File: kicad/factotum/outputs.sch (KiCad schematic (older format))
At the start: 69 parts, among them J10 OUT3, J11 OUT5, J12 OUT7, J13 Conn_01x10_Female, J14 OUT2, J15 OUT4, J16 OUT6, J17 OUT8, J18 Conn_01x10_Male, J19 Conn_01x18_Female, J20 Conn_01x18_Male, J9 OUT1, U10 DAC128S085, U15 PCA9685PW, U6 LM2902, U7 LM2902

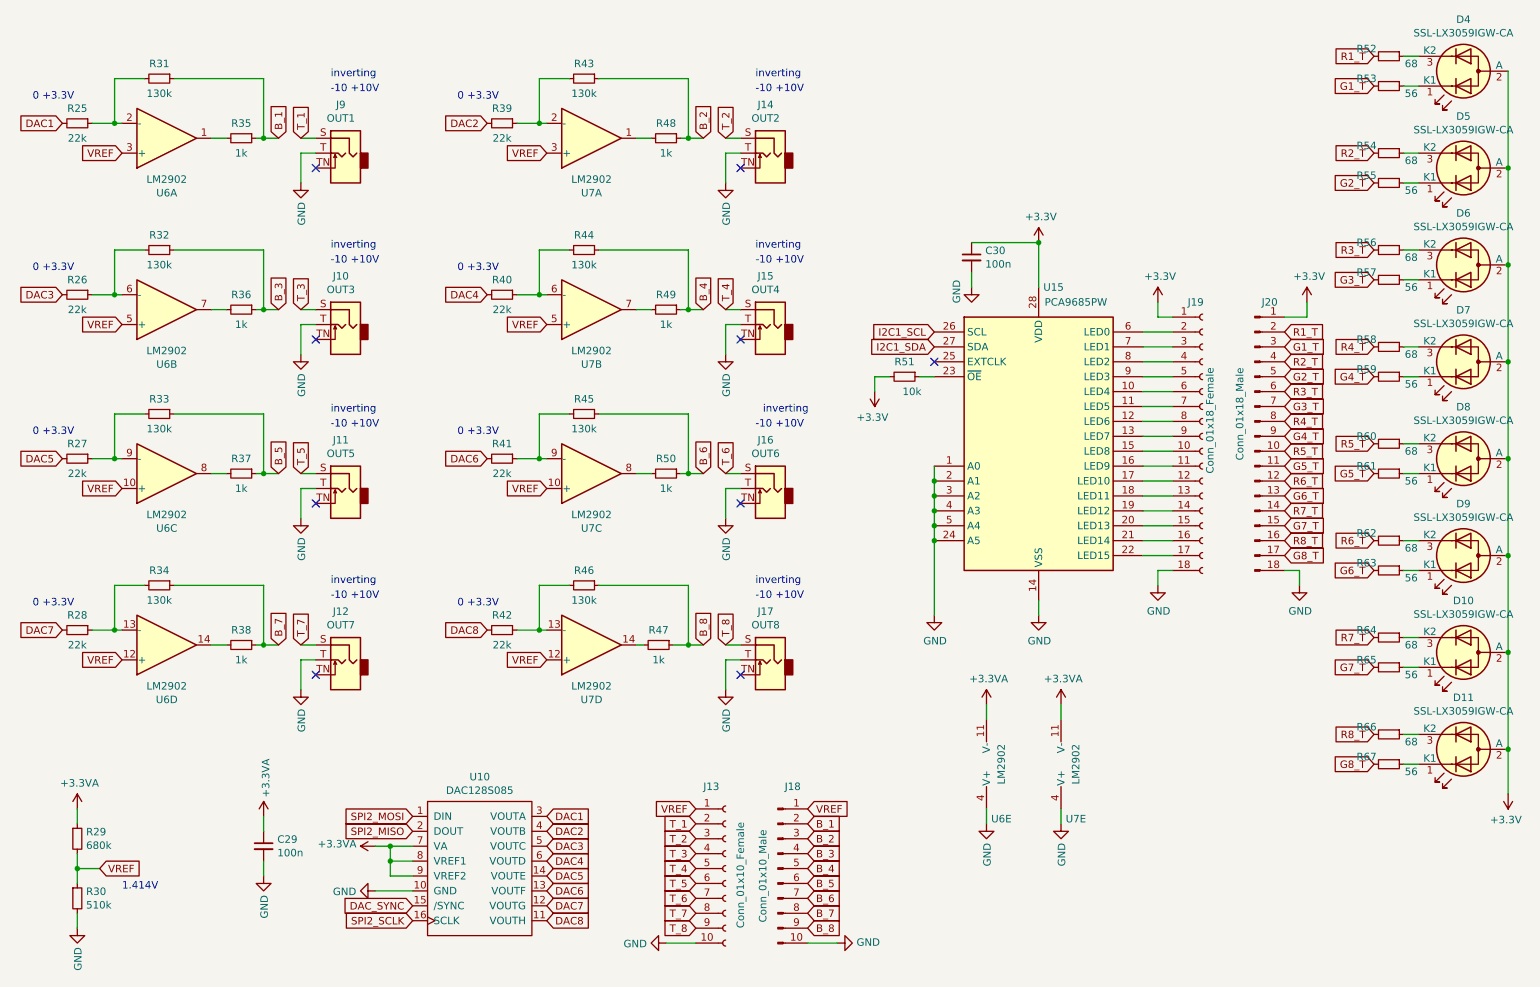
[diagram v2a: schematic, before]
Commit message: inital board layout done but not routed
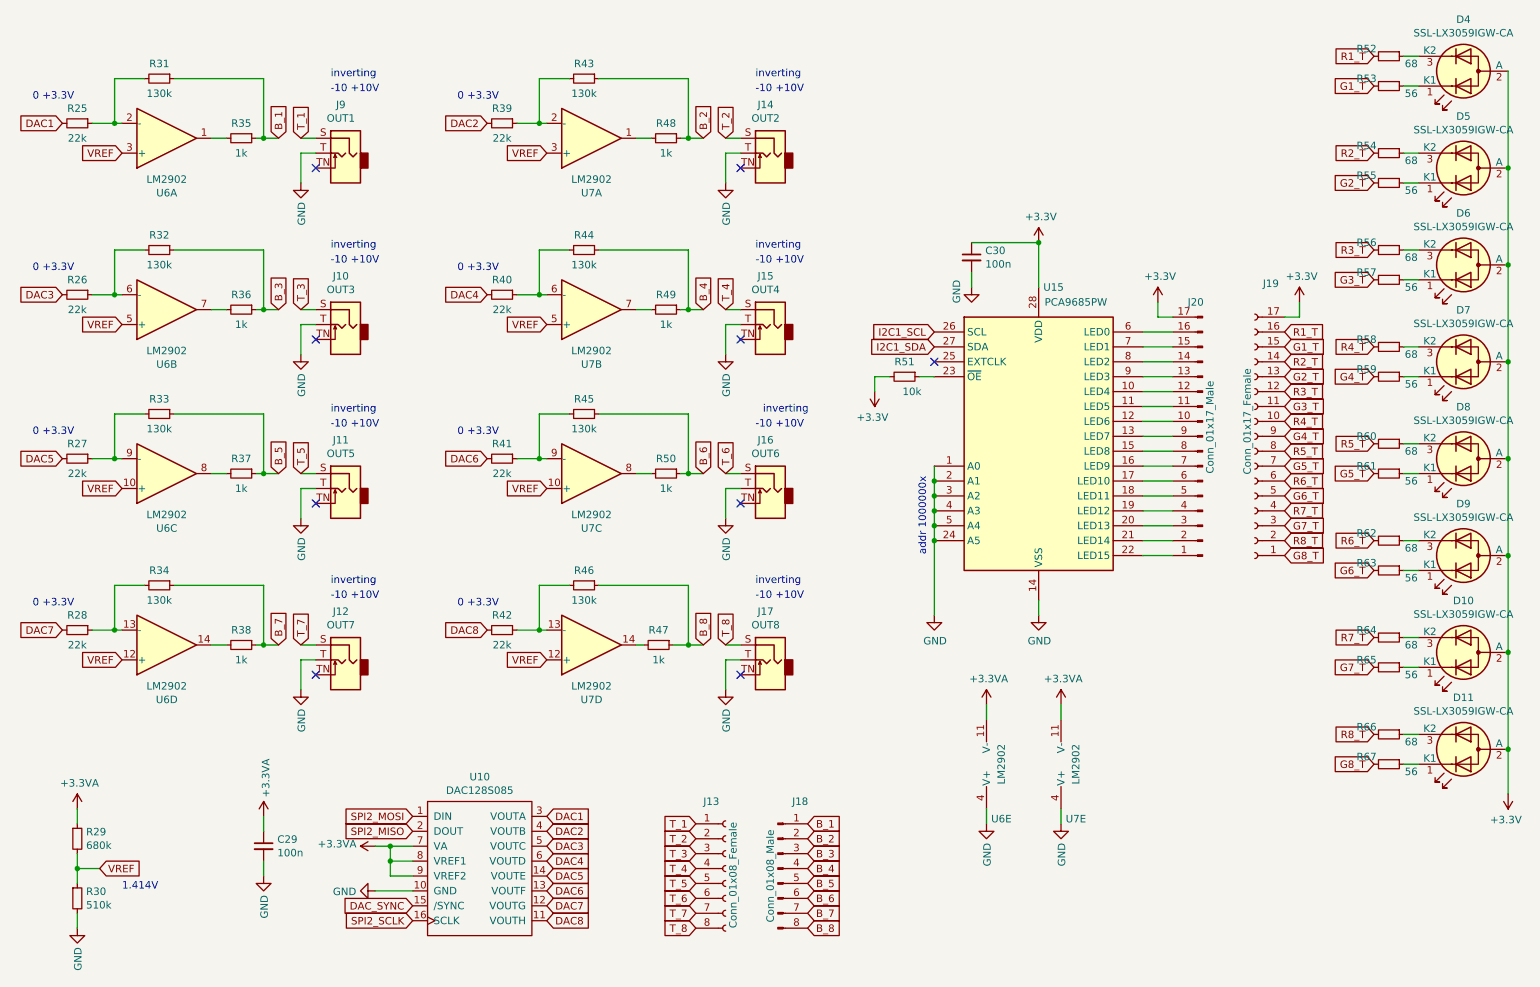
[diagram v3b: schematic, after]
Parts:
- removed J13: Conn_01x10_Female, Connector_PinSocket_1.27mm:PinSocket_1x10_P1.27mm_Vertical, symbol Connector:Conn_01x10_Female
- removed J18: Conn_01x10_Male, Connector_PinHeader_1.27mm:PinHeader_1x10_P1.27mm_Vertical, symbol Connector:Conn_01x10_Male
- removed J19: Conn_01x18_Female, Connector_PinSocket_1.27mm:PinSocket_1x18_P1.27mm_Vertical, symbol Connector:Conn_01x18_Female
- removed J20: Conn_01x18_Male, Connector_PinHeader_1.27mm:PinHeader_1x18_P1.27mm_Vertical, symbol Connector:Conn_01x18_Male
- added J13: Conn_01x08_Female, Connector_PinSocket_2.54mm:PinSocket_1x08_P2.54mm_Vertical, symbol Connector:Conn_01x08_Female
- added J18: Conn_01x08_Male, Connector_PinHeader_2.54mm:PinHeader_1x08_P2.54mm_Vertical, symbol Connector:Conn_01x08_Male
- added J19: Conn_01x17_Female, Connector_PinSocket_2.54mm:PinSocket_1x17_P2.54mm_Vertical, symbol Connector:Conn_01x17_Female
- added J20: Conn_01x17_Male, Connector_PinHeader_2.54mm:PinHeader_1x17_P2.54mm_Vertical, symbol Connector:Conn_01x17_Male
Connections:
- net +3V3: now also J19.17 (Pin_17), J20.17 (Pin_17)
- net B_1: now also J18.1 (Pin_1)
- net B_2: now also J18.2 (Pin_2)
- net B_3: now also J18.3 (Pin_3)
- net B_4: now also J18.4 (Pin_4)
- net B_5: now also J18.5 (Pin_5)
- net B_6: now also J18.6 (Pin_6)
- net B_7: now also J18.7 (Pin_7)
- net B_8: now also J18.8 (Pin_8)
- net G1_T: now also J19.15 (Pin_15)
- net G2_T: now also J19.13 (Pin_13)
- net G3_T: now also J19.11 (Pin_11)
- net G4_T: now also J19.9 (Pin_9)
- net G5_T: now also J19.7 (Pin_7)
- net G6_T: now also J19.5 (Pin_5)
- net G7_T: now also J19.3 (Pin_3)
- net G8_T: now also J19.1 (Pin_1)
- net R1_T: now also J19.16 (Pin_16)
- net R2_T: now also J19.14 (Pin_14)
- net R3_T: now also J19.12 (Pin_12)
- net R4_T: now also J19.10 (Pin_10)
- net R5_T: now also J19.8 (Pin_8)
- net R6_T: now also J19.6 (Pin_6)
- net R7_T: now also J19.4 (Pin_4)
- net R8_T: now also J19.2 (Pin_2)
- net T_1: now also J13.1 (Pin_1)
- net T_2: now also J13.2 (Pin_2)
- net T_3: now also J13.3 (Pin_3)
- net T_4: now also J13.4 (Pin_4)
- net T_5: now also J13.5 (Pin_5)
- net T_6: now also J13.6 (Pin_6)
- net T_7: now also J13.7 (Pin_7)
- net T_8: now also J13.8 (Pin_8)
- net at U15.15 (LED8): now also J20.8 (Pin_8)
- net at U15.16 (LED9): now also J20.7 (Pin_7)
- net at U15.17 (LED10): now also J20.6 (Pin_6)
- net at U15.18 (LED11): now also J20.5 (Pin_5)
- net at U15.19 (LED12): now also J20.4 (Pin_4)
- net at U15.20 (LED13): now also J20.3 (Pin_3)
- net at U15.21 (LED14): now also J20.2 (Pin_2)
- net at U15.22 (LED15): now also J20.1 (Pin_1)
- net at U15.6 (LED0): now also J20.16 (Pin_16)
- net at U15.7 (LED1): now also J20.15 (Pin_15)
- net at U15.8 (LED2): now also J20.14 (Pin_14)
- net at U15.9 (LED3): now also J20.13 (Pin_13)
- net at U15.10 (LED4): now also J20.12 (Pin_12)
- net at U15.11 (LED5): now also J20.11 (Pin_11)
- net at U15.12 (LED6): now also J20.10 (Pin_10)
- net at U15.13 (LED7): now also J20.9 (Pin_9)
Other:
- note added: "addr 1000000x"
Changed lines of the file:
@@
 Wire Wire Line
 	7000 4100 7000 4600
-$Comp
-L Connector:Conn_01x10_Male J18
-U 1 1 5FE57044
-P 5950 6300
-F 0 "J18" H 6050 6850 50  0000 C CNN
-F 1 "Conn_01x10_Male" V 5850 6250 50  0000 C CNN
-F 2 "Connector_PinHeader_1.27mm:PinHeader_1x10_P1.27mm_Vertical" H 5950 6300 50  0001 C CNN
-F 3 "~" H 5950 6300 50  0001 C CNN
-	1    5950 6300
-	1    0    0    -1
-$EndComp
-$Comp
-L Connector:Conn_01x10_Female J13
-U 1 1 5FE59C5F
-P 5600 6300
-F 0 "J13" H 5450 6850 50  0000 L CNN
-F 1 "Conn_01x10_Female" V 5700 5900 50  0000 L CNN
-F 2 "Connector_PinSocket_1.27mm:PinSocket_1x10_P1.27mm_Vertical" H 5600 6300 50  0001 C CNN
-F 3 "~" H 5600 6300 50  0001 C CNN
-	1    5600 6300
-	1    0    0    -1
-$EndComp
-$Comp
-L power:GND #PWR?
-U 1 1 5FE6B456
-P 5200 6800
-AR Path="/5FE6B456" Ref="#PWR?"  Part="1"
-AR Path="/6088BCB1/5FE6B456" Ref="#PWR073"  Part="1"
-F 0 "#PWR073" H 5200 6550 50  0001 C CNN
-F 1 "GND" V 5205 6672 50  0000 R CNN
-F 2 "" H 5200 6800 50  0001 C CNN
-F 3 "" H 5200 6800 50  0001 C CNN
-	1    5200 6800
-	0    1    1    0
-$EndComp
-$Comp
-L power:GND #PWR?
-U 1 1 5FE6C387
-P 6350 6800
-AR Path="/5FE6C387" Ref="#PWR?"  Part="1"
-AR Path="/6088BCB1/5FE6C387" Ref="#PWR078"  Part="1"
-F 0 "#PWR078" H 6350 6550 50  0001 C CNN
-F 1 "GND" V 6355 6672 50  0000 R CNN
-F 2 "" H 6350 6800 50  0001 C CNN
-F 3 "" H 6350 6800 50  0001 C CNN
-	1    6350 6800
-	0    -1   -1   0
-$EndComp
-Text GLabel 5400 5900 0    50   Input ~ 0
-VREF
-Text GLabel 6150 5900 2    50   Input ~ 0
-VREF
 Wire Wire Line
 	5600 4900 5700 4900
@@
 Text GLabel 6150 6700 2    50   Input ~ 0
 B_8
-Wire Wire Line
-	5200 6800 5400 6800
-Wire Wire Line
-	6150 6800 6350 6800
 Text GLabel 5400 6600 0    50   Input ~ 0
 T_7
@@
 	6600 3000 6600 3100
 NoConn ~ 7000 2900
-$Comp
-L Connector:Conn_01x18_Female J19
-U 1 1 6050DE2F
-P 8800 3400
-F 0 "J19" H 8700 4300 50  0000 L CNN
-F 1 "Conn_01x18_Female" V 8850 3150 50  0000 L CNN
-F 2 "Connector_PinSocket_1.27mm:PinSocket_1x18_P1.27mm_Vertical" H 8800 3400 50  0001 C CNN
-F 3 "~" H 8800 3400 50  0001 C CNN
-	1    8800 3400
-	1    0    0    -1
-$EndComp
-$Comp
-L Connector:Conn_01x18_Male J20
-U 1 1 605120D4
-P 9150 3400
-F 0 "J20" H 9250 4300 50  0000 C CNN
-F 1 "Conn_01x18_Male" V 9050 3550 50  0000 C CNN
-F 2 "Connector_PinHeader_1.27mm:PinHeader_1x18_P1.27mm_Vertical" H 9150 3400 50  0001 C CNN
-F 3 "~" H 9150 3400 50  0001 C CNN
-	1    9150 3400
-	1    0    0    -1
-$EndComp
 Wire Wire Line
 	8400 2700 8600 2700
@@
 Wire Wire Line
 	8600 4200 8400 4200
-$Comp
-L power:GND #PWR085
-U 1 1 605A6321
-P 8500 4400
-F 0 "#PWR085" H 8500 4150 50  0001 C CNN
-F 1 "GND" H 8505 4227 50  0000 C CNN
-F 2 "" H 8500 4400 50  0001 C CNN
-F 3 "" H 8500 4400 50  0001 C CNN
-	1    8500 4400
-	1    0    0    -1
-$EndComp
-Wire Wire Line
-	8600 4300 8500 4300
-Wire Wire Line
-	8500 4300 8500 4400
-$Comp
-L power:+3.3V #PWR084
-U 1 1 605B00A7
-P 8500 2500
-F 0 "#PWR084" H 8500 2350 50  0001 C CNN
-F 1 "+3.3V" H 8515 2673 50  0000 C CNN
-F 2 "" H 8500 2500 50  0001 C CNN
-F 3 "" H 8500 2500 50  0001 C CNN
-	1    8500 2500
-	1    0    0    -1
-$EndComp
-Wire Wire Line
-	8500 2500 8500 2600
-Wire Wire Line
-	8500 2600 8600 2600
 Text GLabel 9350 2700 2    50   Input ~ 0
 R1_T
-$Comp
-L power:+3.3V #PWR087
-U 1 1 605BF2CA
-P 9500 2500
-F 0 "#PWR087" H 9500 2350 50  0001 C CNN
-F 1 "+3.3V" H 9515 2673 50  0000 C CNN
-F 2 "" H 9500 2500 50  0001 C CNN
-F 3 "" H 9500 2500 50  0001 C CNN
-	1    9500 2500
-	1    0    0    -1
-$EndComp
-Wire Wire Line
-	9350 2600 9500 2600
-Wire Wire Line
-	9500 2600 9500 2500
-$Comp
-L power:GND #PWR086
-U 1 1 605C96BF
-P 9450 4400
-F 0 "#PWR086" H 9450 4150 50  0001 C CNN
-F 1 "GND" H 9455 4227 50  0000 C CNN
-F 2 "" H 9450 4400 50  0001 C CNN
-F 3 "" H 9450 4400 50  0001 C CNN
-	1    9450 4400
-	1    0    0    -1
-$EndComp
-Wire Wire Line
-	9350 4300 9450 4300
-Wire Wire Line
-	9450 4300 9450 4400
 Text GLabel 9350 2800 2    50   Input ~ 0
 G1_T
@@
 Wire Wire Line
 	7250 2400 7250 2300
+Text Notes 6950 4200 1    50   ~ 0
+addr 1000000x
+$Comp
+L Connector:Conn_01x08_Female J13
+U 1 1 600EC710
+P 5600 6300
+F 0 "J13" H 5450 6750 50  0000 L CNN
+F 1 "Conn_01x08_Female" V 5650 5900 50  0000 L CNN
+F 2 "Connector_PinSocket_2.54mm:PinSocket_1x08_P2.54mm_Vertical" H 5600 6300 50  0001 C CNN
+F 3 "~" H 5600 6300 50  0001 C CNN
+	1    5600 6300
+	1    0    0    -1
+$EndComp
+$Comp
+L Connector:Conn_01x08_Male J18
+U 1 1 6010E502
+P 5950 6300
+F 0 "J18" H 6100 6750 50  0000 C CNN
+F 1 "Conn_01x08_Male" V 5900 6250 50  0000 C CNN
+F 2 "Connector_PinHeader_2.54mm:PinHeader_1x08_P2.54mm_Vertical" H 5950 6300 50  0001 C CNN
+F 3 "~" H 5950 6300 50  0001 C CNN
+	1    5950 6300
+	1    0    0    -1
+$EndComp
+$Comp
+L power:+3.3V #PWR0101
+U 1 1 602A7C6E
+P 8500 2500
+F 0 "#PWR0101" H 8500 2350 50  0001 C CNN
+F 1 "+3.3V" H 8515 2673 50  0000 C CNN
+F 2 "" H 8500 2500 50  0001 C CNN
+F 3 "" H 8500 2500 50  0001 C CNN
+	1    8500 2500
+	1    0    0    -1
+$EndComp
+$Comp
+L power:+3.3V #PWR0102
+U 1 1 602A8C1D
+P 9450 2500
+F 0 "#PWR0102" H 9450 2350 50  0001 C CNN
+F 1 "+3.3V" H 9465 2673 50  0000 C CNN
+F 2 "" H 9450 2500 50  0001 C CNN
+F 3 "" H 9450 2500 50  0001 C CNN
+	1    9450 2500
+	1    0    0    -1
+$EndComp
+$Comp
+L Connector:Conn_01x17_Female J19
+U 1 1 602C2934
+P 9150 3400
+F 0 "J19" H 9042 2375 50  0000 C CNN
+F 1 "Conn_01x17_Female" V 9200 3300 50  0000 C CNN
+F 2 "Connector_PinSocket_2.54mm:PinSocket_1x17_P2.54mm_Vertical" H 9150 3400 50  0001 C CNN
+F 3 "~" H 9150 3400 50  0001 C CNN
+	1    9150 3400
+	-1   0    0    1
+$EndComp
+$Comp
+L Connector:Conn_01x17_Male J20
+U 1 1 602D94E3
+P 8800 3400
+F 0 "J20" H 8900 2500 50  0000 R CNN
+F 1 "Conn_01x17_Male" V 8750 3650 50  0000 R CNN
+F 2 "Connector_PinHeader_2.54mm:PinHeader_1x17_P2.54mm_Vertical" H 8800 3400 50  0001 C CNN
+F 3 "~" H 8800 3400 50  0001 C CNN
+	1    8800 3400
+	-1   0    0    1
+$EndComp
+Wire Wire Line
+	9350 2600 9450 2600
+Wire Wire Line
+	9450 2600 9450 2500
+Wire Wire Line
+	8600 2600 8500 2600
+Wire Wire Line
+	8500 2600 8500 2500
 $EndSCHEMATC

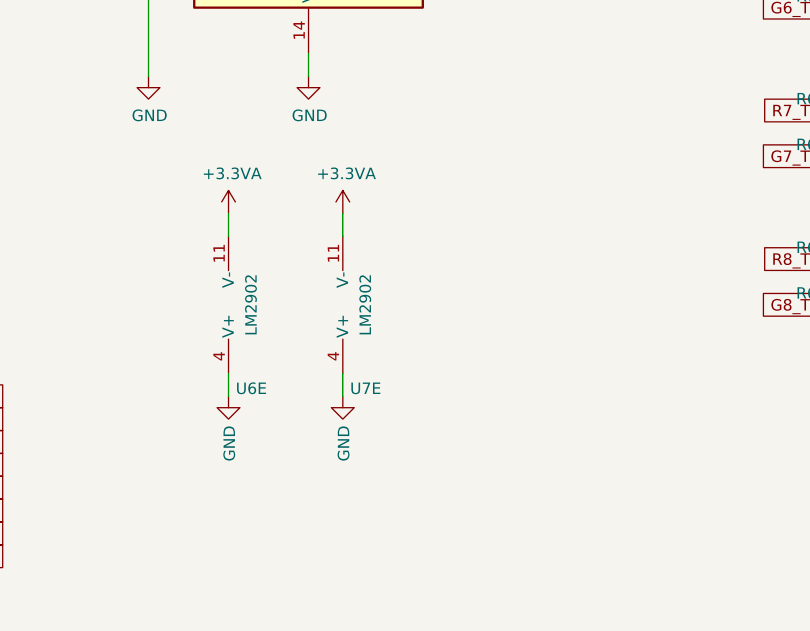
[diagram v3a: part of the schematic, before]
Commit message: adding switches to inputs; fixing resistor components to 603
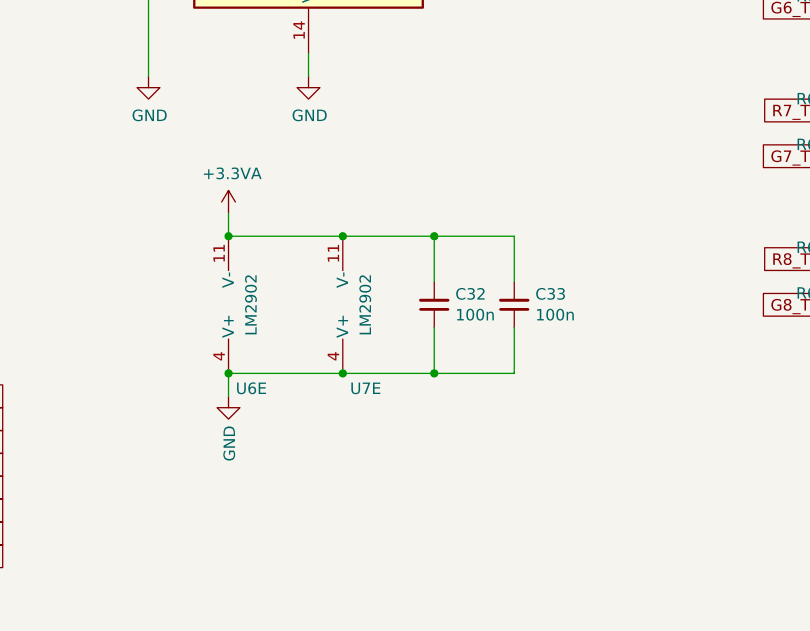
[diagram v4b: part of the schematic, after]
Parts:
- added C32, C33: 100n, Capacitor_SMD:C_0603_1608Metric_Pad1.08x0.95mm_HandSolder, symbol Device:C_Small
- R25, R26, R27, R28, R29, R30, R31, R32, R33, R34, R35, R36, R37, R38, R39, R40, R41, R42, R43, R44, R45, R46, R47, R48, R49, R50, R51, R52, R53, R54, R55, R56, R57, R58, R59, R60, R61, R62, R63, R64, R65, R66, R67: footprint Resistor_SMD:R_0201_0603Metric_Pad0.64x0.40mm_HandSolder -> Resistor_SMD:R_0603_1608Metric_Pad0.98x0.95mm_HandSolder
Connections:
- net +3.3VA: now also C32.2, C33.2
- net GND: now also C32.1, C33.1
